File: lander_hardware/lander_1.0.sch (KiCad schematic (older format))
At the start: 25 parts, among them IC1 ATMEGA328-P, J1 Power Connector, P1 Power Supplement, P2 XBEE Out, P3 Digital Supplement 1, P4 Digital Supplement 2, P5 Analog Supplement, U1 LD1117S33TR, U2 7805, U3 DHT11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

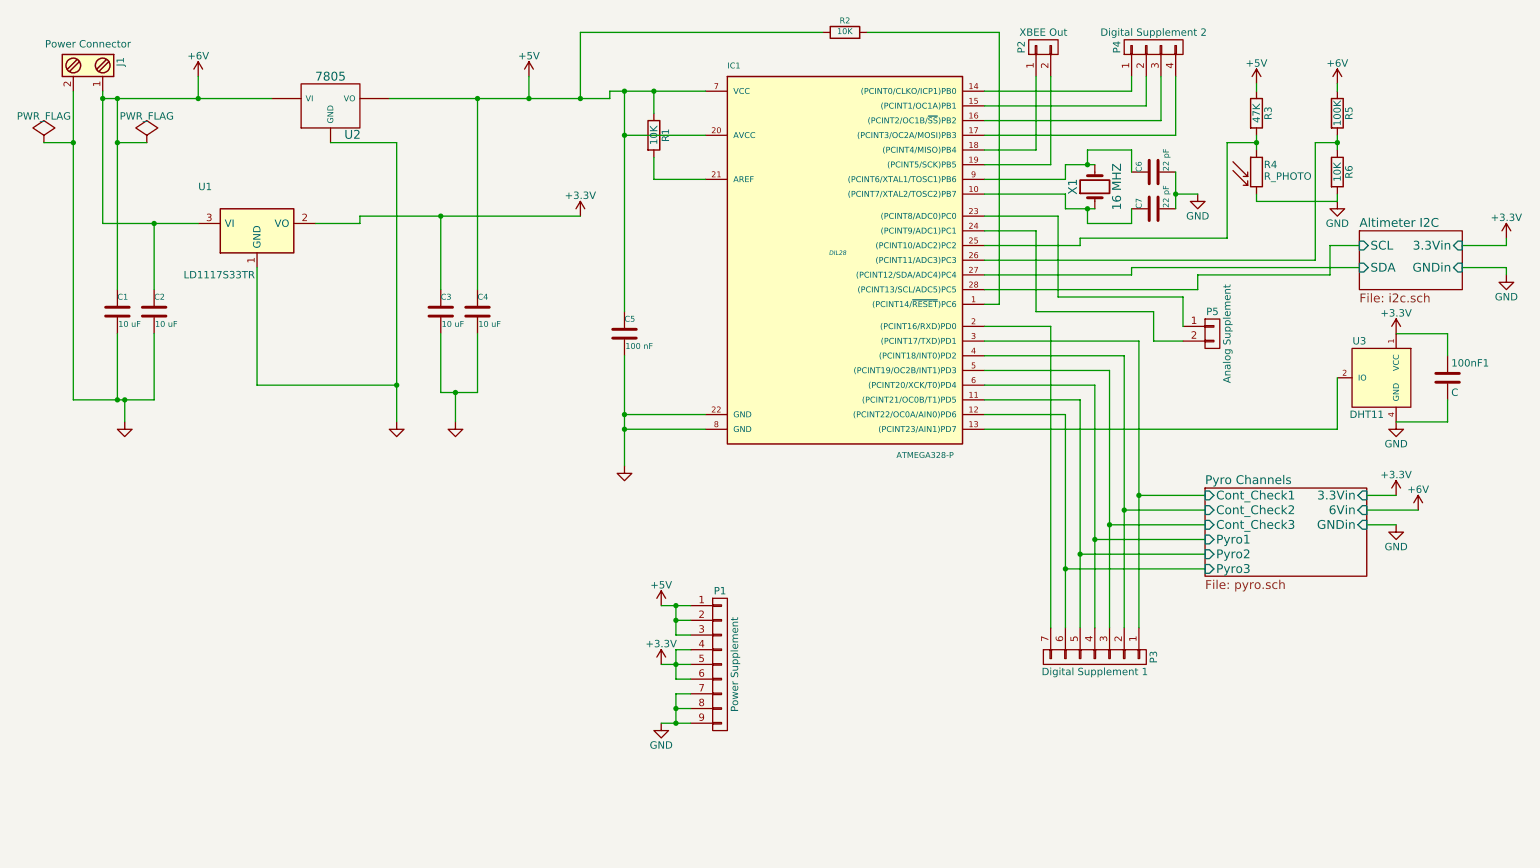
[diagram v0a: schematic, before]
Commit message: Added ICSP
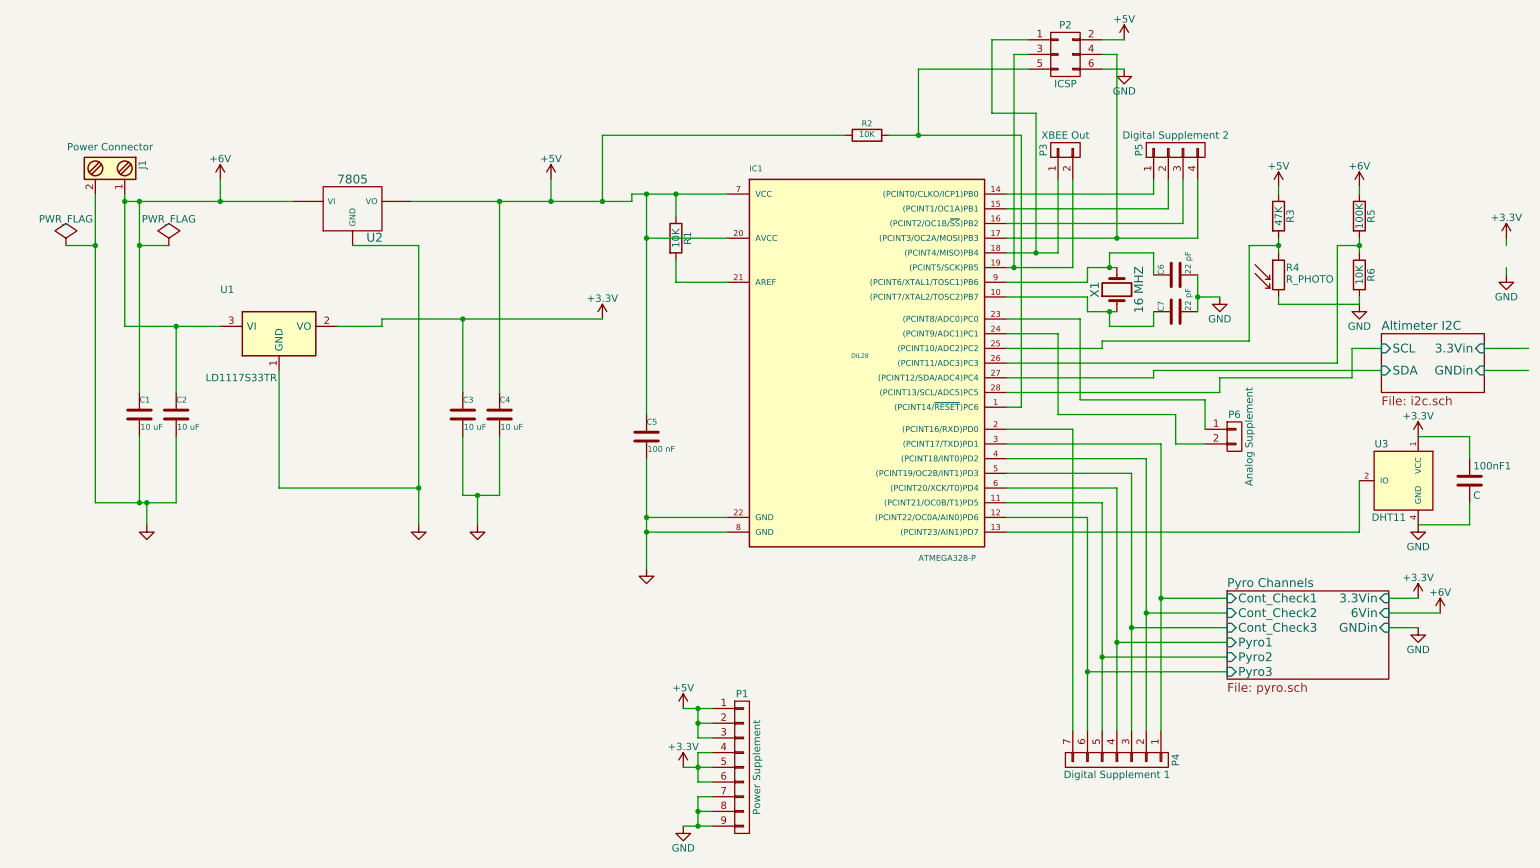
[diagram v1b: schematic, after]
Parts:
- added P2: ICSP, symbol CONN_02X03
- renumbered P2 to P3, P3 to P4, P4 to P5, P5 to P6
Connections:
- net +5V: now also P2.2 (P2)
- net GND: now also P2.6 (P6)
- net at IC1.1 ((PCINT14/~RESET~)PC6), R2.2: now also P2.5 (P5)
- net at IC1.17 ((PCINT3/OC2A/MOSI)PB3), P5.4 (P4): now also P2.4 (P4)
- net at IC1.18 ((PCINT4/MISO)PB4), P3.1 (P1): now also P2.1 (P1)
- net at IC1.19 ((PCINT5/SCK)PB5), P3.2 (P2): now also P2.3 (P3)
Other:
- moved on the sheet: 100nF1, C1, C2, C3, C4, C5, C6, C7, IC1, J1, P1, P3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
